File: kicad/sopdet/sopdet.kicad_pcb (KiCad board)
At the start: 4 copper layers, 30.5 x 52.8 mm, 45 parts, among them J1 IPEX_MHF1, J2 IPEX_MHF1, Q1 Q_PMOS_GSD, U1 Power_Connector, U2 AP63301WU-7, U3 RFM95W-915S2, U4 LC29H (DA), U5 Pi Zero 2W

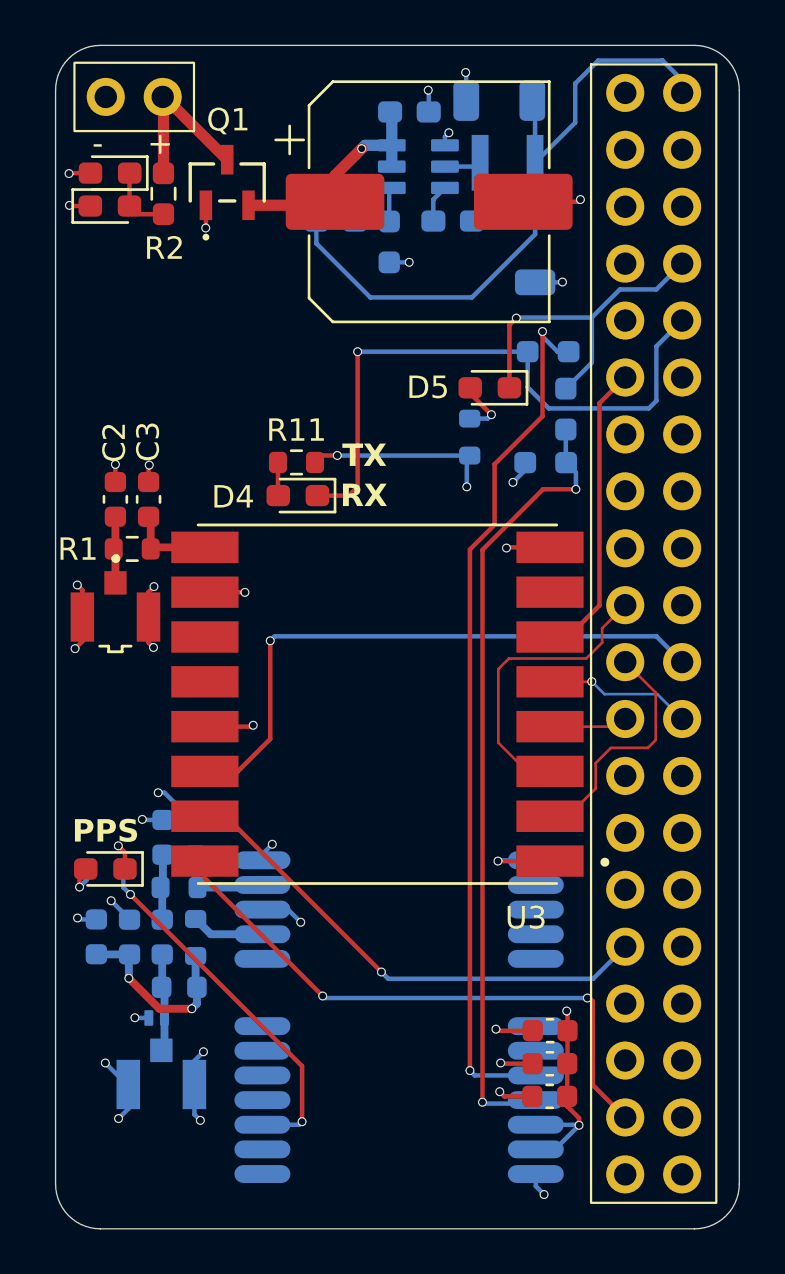
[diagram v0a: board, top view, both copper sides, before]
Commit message: Finish Sopdet routing
Also add logos for Sirius and Sopdet
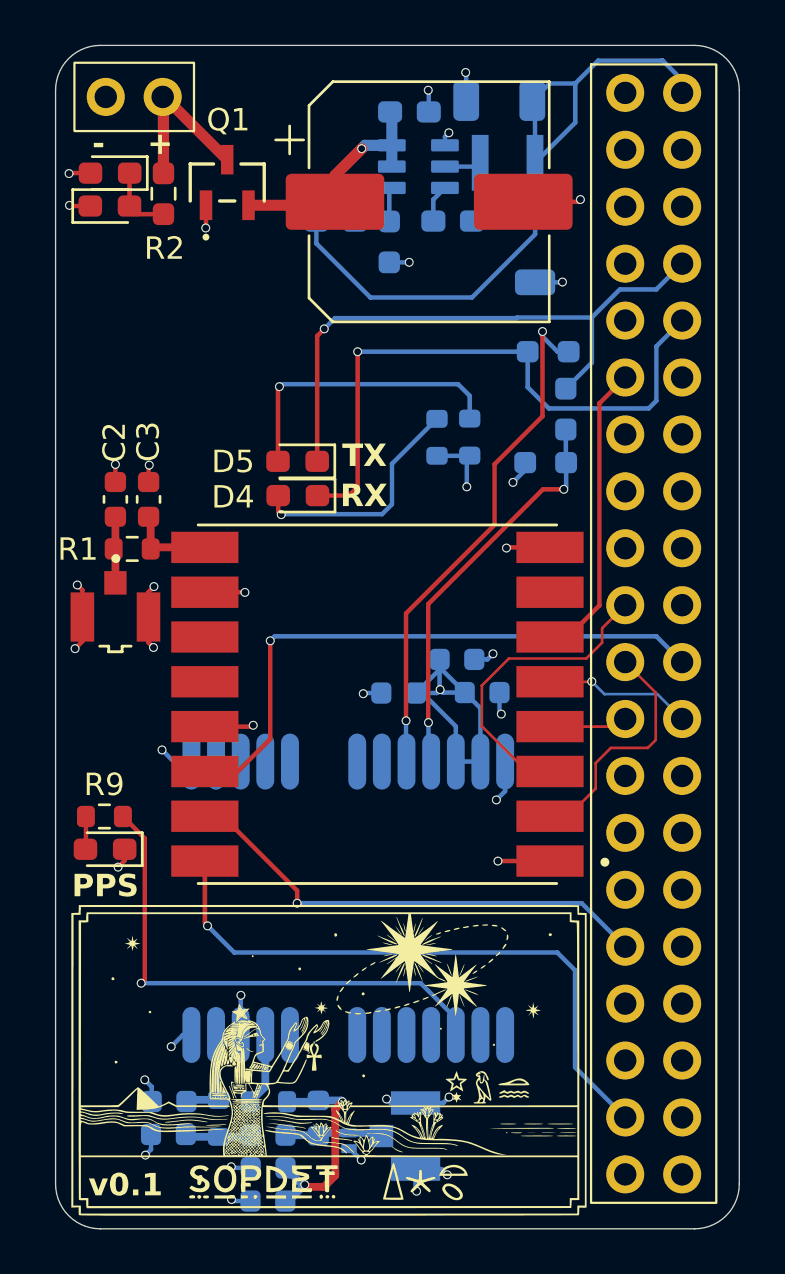
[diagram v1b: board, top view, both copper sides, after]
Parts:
- added G***: LOGO, sirius:sopdet_logo, F.Cu at (138.2, 87.0)
- C14, C15, C16, R11: moved to B.Cu
- R9: moved to F.Cu
- moved C16 18.5 mm to (143.9, 69.2), turned to 180 degrees
- moved C15 18.3 mm to (145.1, 70.7), turned to 180 degrees
- moved C14 16.5 mm to (141.3, 70.7)
- moved C12 14.1 mm to (135.5, 93.3), turned to 180 degrees
- moved C10 13.3 mm to (131.1, 90.4), turned to 0 degrees
- moved C13 12.0 mm to (135.5, 91.9), turned to 180 degrees
- moved C9 11.8 mm to (131.1, 88.9), turned to 0 degrees
- moved J2 11.6 mm to (142.1, 90.4), turned to 90 degrees
- moved R5 10.5 mm to (133.3, 89.7), turned to -90 degrees
- moved D3 10.2 mm to (139.1, 90.7), turned to -90 degrees
- moved C11 10.0 mm to (135.5, 90.4), turned to 0 degrees
- moved D5 9.18 mm to (136.8, 60.3)
- moved L2 8.52 mm to (137.8, 89.6), turned to 90 degrees
- moved R6 8.02 mm to (135.5, 88.9), turned to 180 degrees
- moved R11 6.37 mm to (143.1, 59.3), turned to -90 degrees
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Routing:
- net /Pi_TX_2_8: track 35.3 -> 18.0 mm
- net Net-(U4-TXD1): track 39.0 -> 23.4 mm
- net /Pi_TX: track 15.3 -> 27.3 mm
- net Net-(D5-A): track 2.63 -> 13.2 mm
- net Net-(D4-A): track 1.48 -> 10.7 mm, vias 0 -> 1
- net +3V3: track 85.2 -> 76.4 mm, vias 5 -> 3
- net /PPS: track 16.4 -> 23.3 mm, vias 2 -> 1
- net GND: track 48.9 -> 45.4 mm, vias 35 -> 36
- net +5V: track 33.4 -> 35.6 mm
- net /GPIO26: track 26.1 -> 27.7 mm, vias 2 -> 1
- net Net-(C12-Pad1): track 8.41 -> 9.90 mm
- net /MOSI_SPI0: track 13.3 -> 14.0 mm
- net Net-(D6-A): track 1.86 -> 1.47 mm, vias 1 -> 0
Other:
- board text added: "v0.1"

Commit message: Replace footprint of u.fl connector & screw terminal
Redesign board to accomodate larger footprint, make Sopdet a little smaller to qualify for $2 jlcpcb price, assign Digikey PN to all components, add a script which combines the BOM's of both boards so Digikey can more accurately detect cost savings
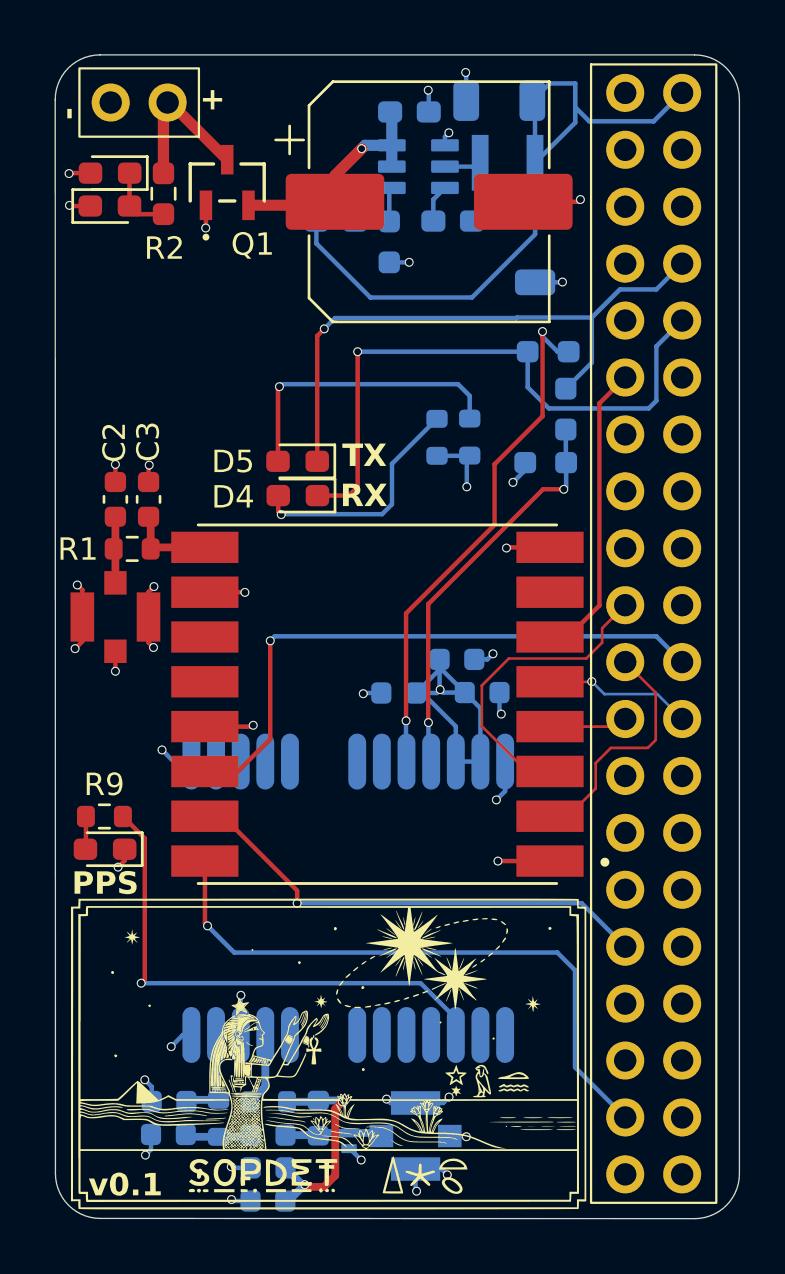
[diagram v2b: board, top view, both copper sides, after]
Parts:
- J1, J2: footprint sirius:ipex_mhf1 -> sirius:TE_CONMHF1-SMD-T
- moved U1 0.33 mm to (129.8, 44.3)
- moved G*** 0.28 mm to (138.2, 86.8)
- turned J1 to 0 degrees
- turned J2 to -90 degrees
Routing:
- net GND: track 45.4 -> 47.0 mm, vias 36 -> 38
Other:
- board size 30.5 x 52.8 mm -> 30.5 x 51.9 mm
